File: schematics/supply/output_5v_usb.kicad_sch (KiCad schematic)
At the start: 88 parts, among them J2 USB_A, Q3 40N06, U10 IRS2153S, U11 CHY100, U12 LM2904, U13 LM2904, U15 LM2904, U16 AMS1117-3.3, U2 EL817, U3 TL431DBV, U4 TL431DBV, U6 INA3221, U8 MC34063AD

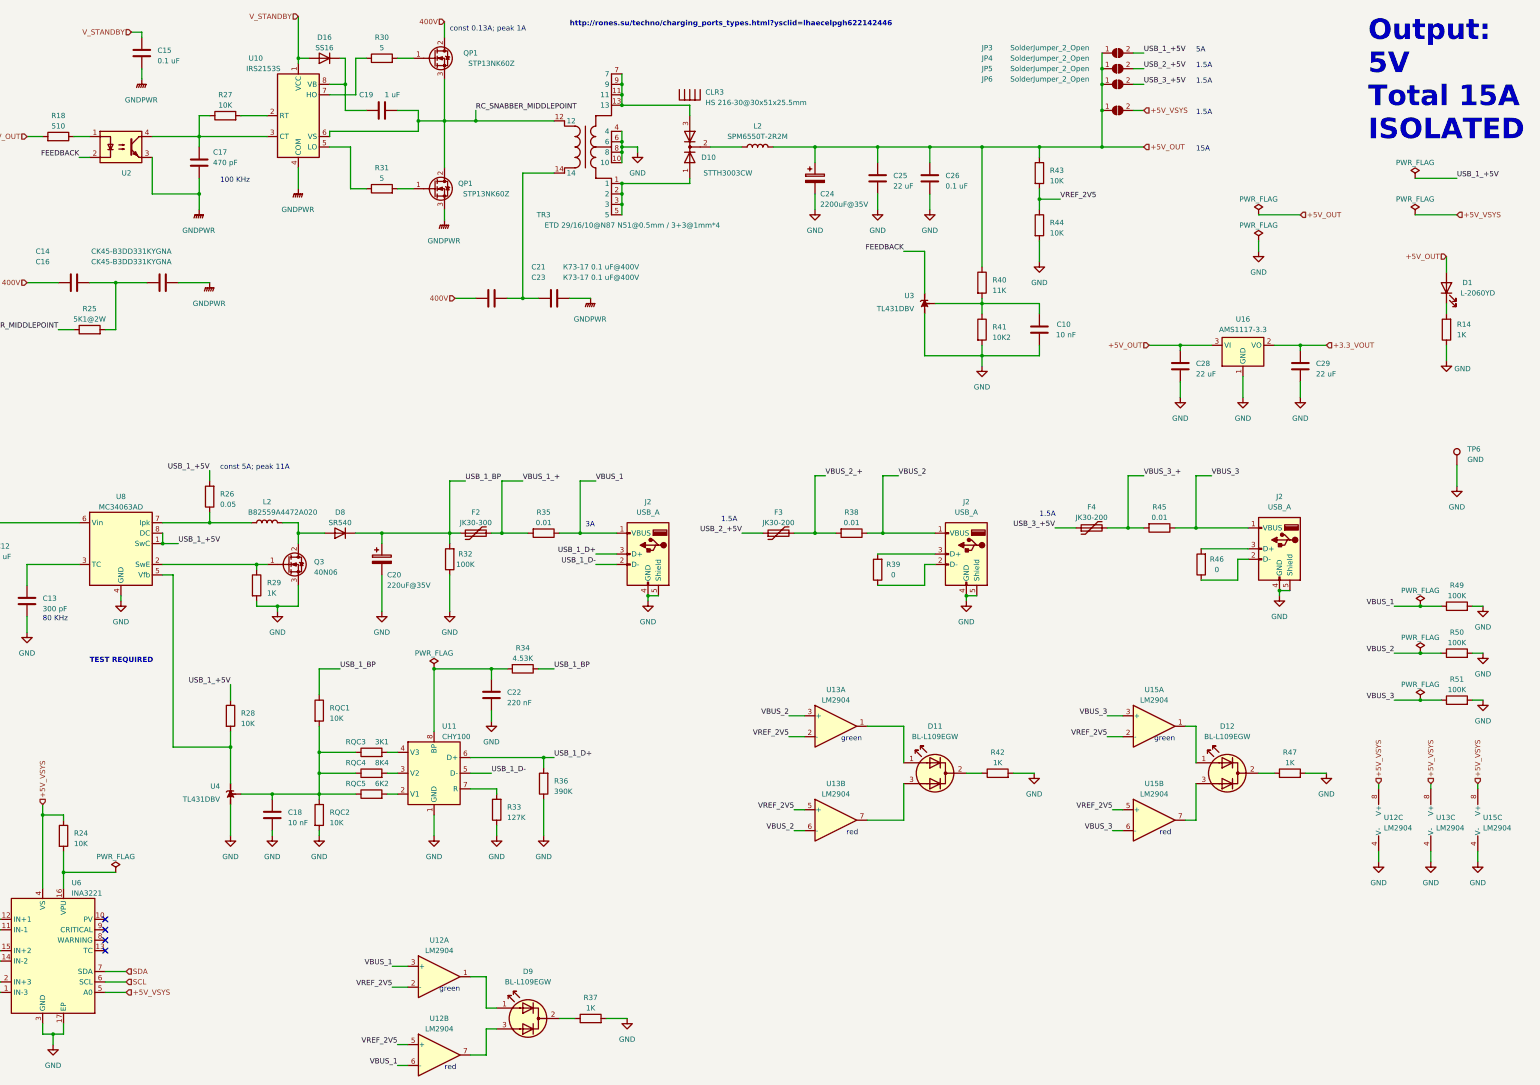
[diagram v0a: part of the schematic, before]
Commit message: prepare to replace ina228 to attiny16+ina169(?). ina228 is an intresting chip, but its too expensive and Im not sure I can buy it on ali
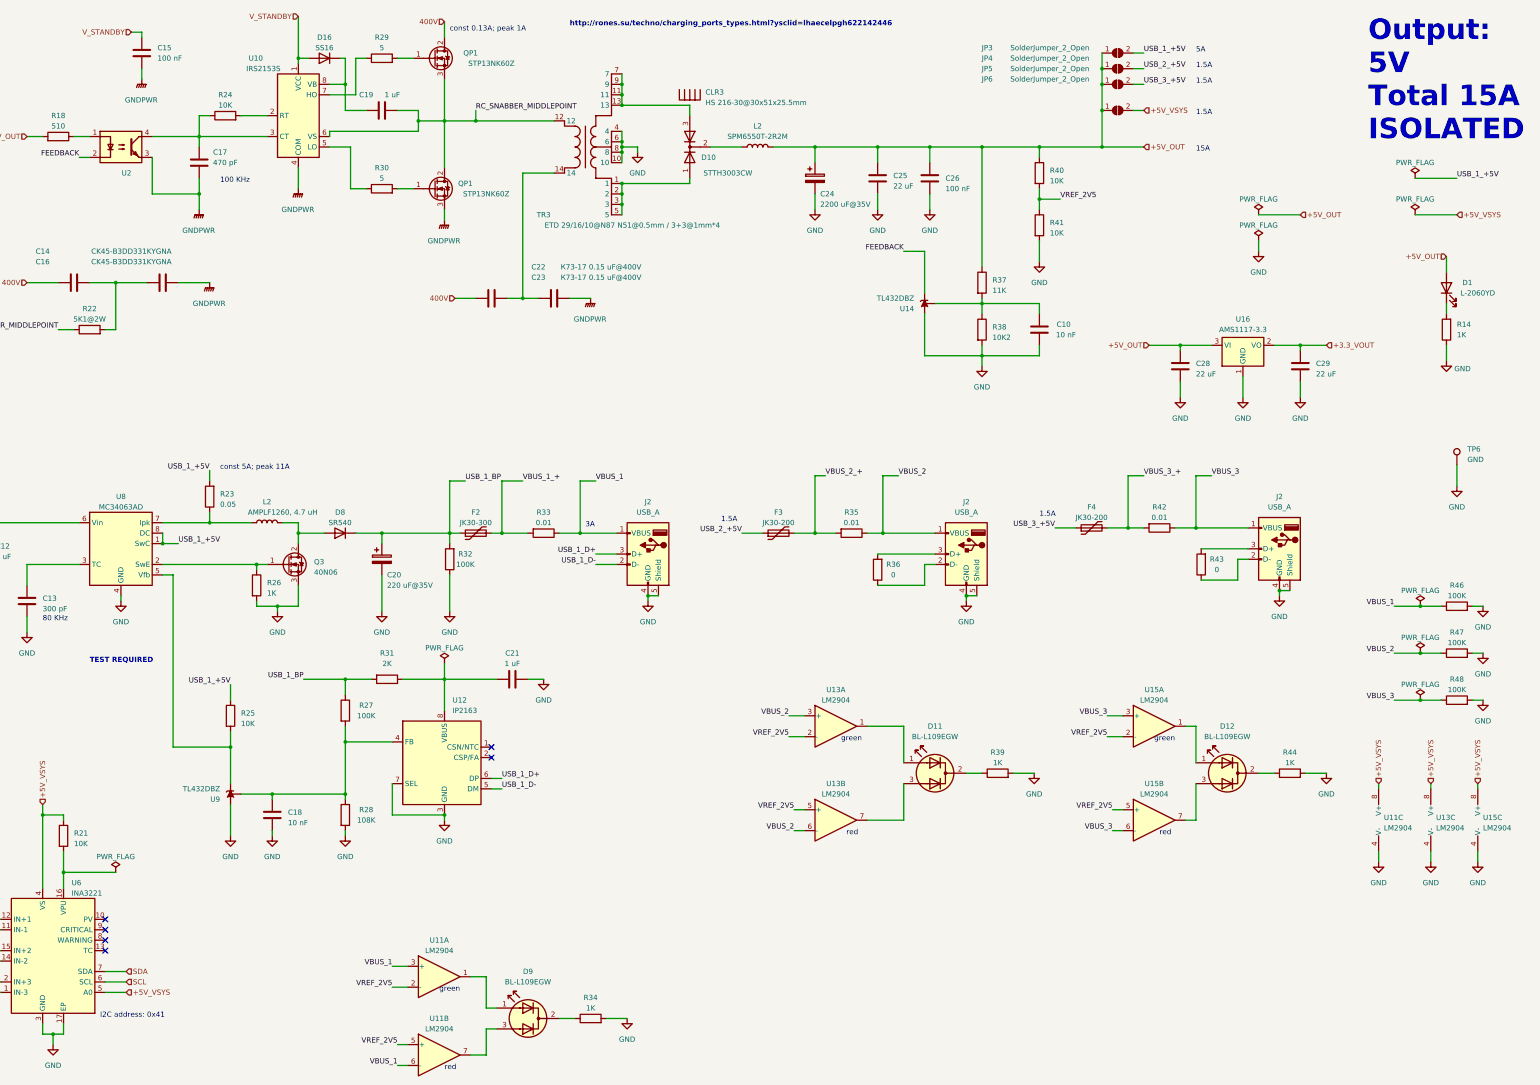
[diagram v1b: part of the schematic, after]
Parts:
- removed C22: 220 nF, Capacitor_SMD:C_0603_1608Metric, symbol Device:C
- removed R33: 127K, Resistor_SMD:R_0805_2012Metric, symbol Device:R
- removed R34: 4.53K, Resistor_SMD:R_0805_2012Metric, symbol Device:R
- removed R36: 390K, Resistor_SMD:R_0805_2012Metric, symbol Device:R
- removed RQC1, RQC2: 10K, Resistor_SMD:R_0805_2012Metric, symbol Device:R
- removed RQC3: 3K1, Resistor_SMD:R_0805_2012Metric, symbol Device:R
- removed RQC4: 8K4, Resistor_SMD:R_0805_2012Metric, symbol Device:R
- removed RQC5: 6K2, Resistor_SMD:R_0805_2012Metric, symbol Device:R
- removed U11: CHY100, Package_SO:SO-8_3.9x4.9mm_P1.27mm, symbol My_Library:CHY100
- removed U3, U4: TL431DBV, Package_TO_SOT_SMD:SOT-23-5, symbol Reference_Voltage:TL431DBV
- added C21: 1 uF, Capacitor_SMD:C_0603_1608Metric, symbol Device:C
- added R27: 100K, Resistor_SMD:R_0805_2012Metric, symbol Device:R
- added R28: 108K, Resistor_SMD:R_0805_2012Metric, symbol Device:R
- added R31: 2K, Resistor_SMD:R_0805_2012Metric, symbol Device:R
- added U12: IP2163, Package_SO:SOP-8_3.9x4.9mm_P1.27mm, symbol My_Library:IP2163
- added U14, U9: TL432DBZ, Package_TO_SOT_SMD:SOT-23-3, symbol Reference_Voltage:TL432DBZ
- C15, C26: value 0.1 uF -> 100 nF
- C20: value 220uF@35V -> 220 uF@35V
- C22: renamed from C21; value К73-17 0.1 uF@400V -> К73-17 0.15 uF@400V; footprint Capacitor_THT:C_Rect_L11.0mm_W6.3mm_P10.00mm_MKT -> Capacitor_THT:C_Rect_L16.5mm_W7.3mm_P15.00mm_MKT
- C23: value К73-17 0.1 uF@400V -> К73-17 0.15 uF@400V; footprint Capacitor_THT:C_Rect_L11.0mm_W6.3mm_P10.00mm_MKT -> Capacitor_THT:C_Rect_L16.5mm_W7.3mm_P15.00mm_MKT
- C24: value 2200uF@35V -> 2200 uF@35V
- D8: footprint Diode_THT:D_DO-27_P5.08mm_Vertical_KathodeUp -> Diode_THT:D_DO-201AD_P3.81mm_Vertical_KathodeUp
- L2: value B82559A4472A020 -> AMPLF1260, 4.7 uH; footprint Library:ERU 20 -> Inductor_SMD:L_TaiTech_TMPC1265_13.5x12.5mm
- U8: footprint Package_SO:SOIC-8_3.9x4.9mm_P1.27mm -> Package_SO:SOP-8_3.9x4.9mm_P1.27mm
- renumbered R24 to R21, R25 to R22, R26 to R23, R27 to R24, R28 to R25, R29 to R26, R30 to R29, R31 to R30, R35 to R33, R37 to R34, R38 to R35, R39 to R36, R40 to R37, R41 to R38, R42 to R39, R43 to R40, R44 to R41, R45 to R42, R46 to R43, R47 to R44, R49 to R46, R50 to R47, R51 to R48, U12 to U11
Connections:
- net FEEDBACK: now also U14.2 (K)
- net GND: now also C21.1, R28.2, U12.3 (GND), U12.7 (SEL), U14.3 (A), U9.3 (A)
- net USB_1_BP: now also R27.1, R31.2
- net USB_1_D+: now also U12.6 (DP)
- net USB_1_D-: now also U12.5 (DM)
- net at C18.2: now also R27.2, R28.1, U12.4 (FB), U9.1 (REF)
- net at R25.2, U8.5 (Vfb): now also U9.2 (K)
- net at C10.2, R37.2, R38.1: now also U14.1 (REF)
- new net: C21.2, R31.1, U12.8 (VBUS)
- no-connect marks 4 -> 6
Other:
- note added: "I2C address: 0x41"

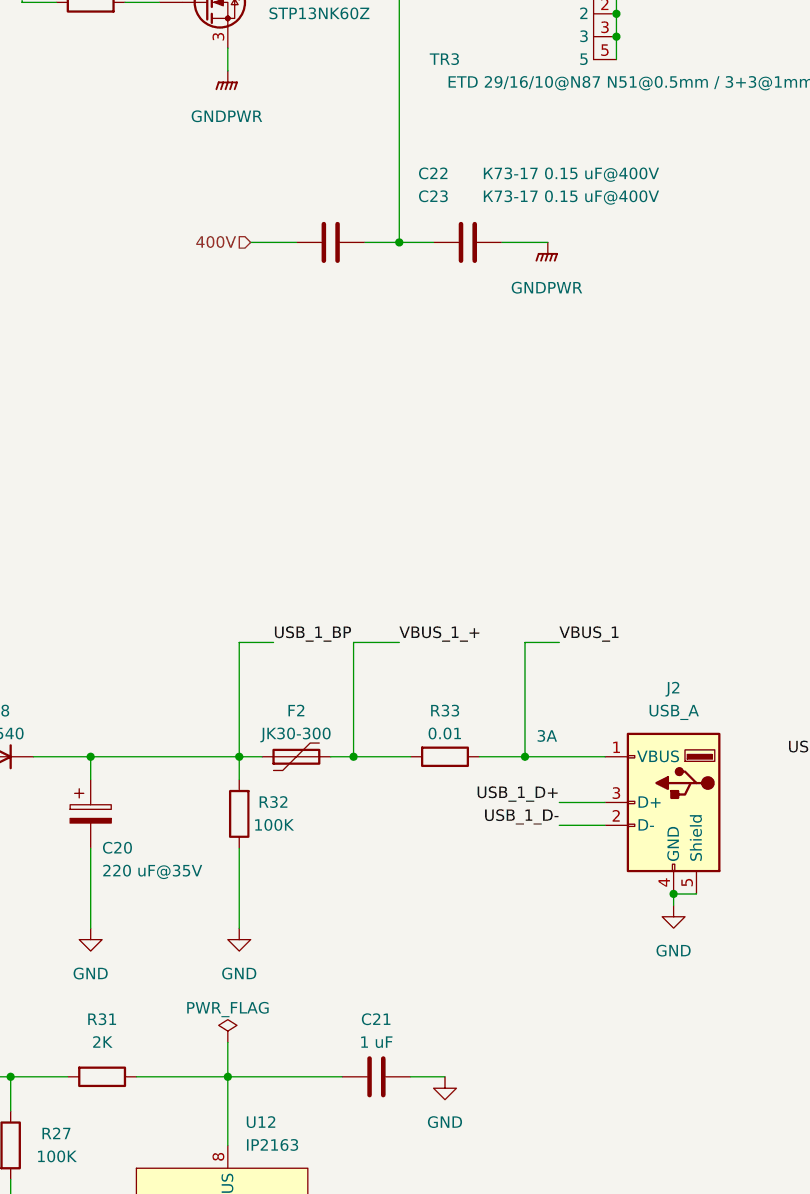
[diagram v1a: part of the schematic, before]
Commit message: Prepare to move USB ports to a few millimenters outside
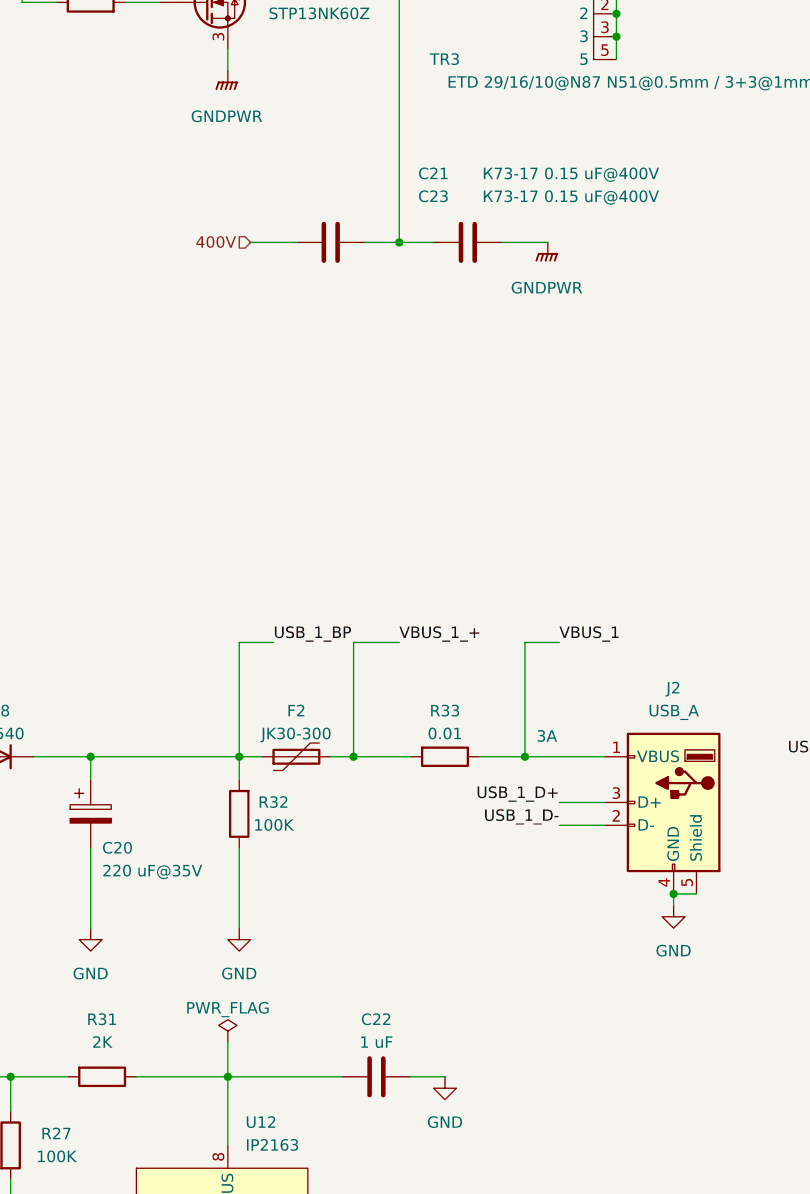
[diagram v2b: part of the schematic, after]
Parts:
- renumbered C22 to C21, C21 to C22
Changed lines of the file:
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@@
   (symbol (lib_id "Device:C") (at 156.21 85.09 270) (unit 1)
     (in_bom yes) (on_board yes) (dnp no)
-    (property "Reference" "C22" (at 167.64 77.47 90)
+    (property "Reference" "C21" (at 167.64 77.47 90)
       (effects (font (size 1.27 1.27)))
     )
@@
       (project "supply"
         (path "/1e139717-fcd1-4008-a6ea-4c993845e928/bcabd54f-a555-4409-9a4f-89c20a3d7682"
-          (reference "C22") (unit 1)
+          (reference "C21") (unit 1)
         )
       )
@@
   (symbol (lib_id "power:PWR_FLAG") (at 381 55.88 0) (unit 1)
     (in_bom yes) (on_board yes) (dnp no) (fields_autoplaced)
-    (property "Reference" "#FLG011" (at 381 53.975 0)
+    (property "Reference" "#FLG012" (at 381 53.975 0)
       (effects (font (size 1.27 1.27)) hide)
     )
@@
       (project "supply"
         (path "/1e139717-fcd1-4008-a6ea-4c993845e928/bcabd54f-a555-4409-9a4f-89c20a3d7682"
-          (reference "#FLG011") (unit 1)
+          (reference "#FLG012") (unit 1)
         )
       )
@@
   (symbol (lib_id "power:PWR_FLAG") (at 342.9 71.12 0) (unit 1)
     (in_bom yes) (on_board yes) (dnp no) (fields_autoplaced)
-    (property "Reference" "#FLG010" (at 342.9 69.215 0)
+    (property "Reference" "#FLG011" (at 342.9 69.215 0)
       (effects (font (size 1.27 1.27)) hide)
     )
@@
       (project "supply"
         (path "/1e139717-fcd1-4008-a6ea-4c993845e928/bcabd54f-a555-4409-9a4f-89c20a3d7682"
-          (reference "#FLG010") (unit 1)
+          (reference "#FLG011") (unit 1)
         )
       )
@@
   (symbol (lib_id "power:PWR_FLAG") (at 382.27 160.02 0) (unit 1)
     (in_bom yes) (on_board yes) (dnp no) (fields_autoplaced)
-    (property "Reference" "#FLG013" (at 382.27 158.115 0)
+    (property "Reference" "#FLG014" (at 382.27 158.115 0)
       (effects (font (size 1.27 1.27)) hide)
     )
@@
       (project "supply"
         (path "/1e139717-fcd1-4008-a6ea-4c993845e928/bcabd54f-a555-4409-9a4f-89c20a3d7682"
-          (reference "#FLG013") (unit 1)
+          (reference "#FLG014") (unit 1)
         )
       )
@@
   (symbol (lib_id "power:PWR_FLAG") (at 342.9 64.77 0) (unit 1)
     (in_bom yes) (on_board yes) (dnp no) (fields_autoplaced)
-    (property "Reference" "#FLG09" (at 342.9 62.865 0)
+    (property "Reference" "#FLG010" (at 342.9 62.865 0)
       (effects (font (size 1.27 1.27)) hide)
     )
@@
       (project "supply"
         (path "/1e139717-fcd1-4008-a6ea-4c993845e928/bcabd54f-a555-4409-9a4f-89c20a3d7682"
-          (reference "#FLG09") (unit 1)
+          (reference "#FLG010") (unit 1)
         )
       )
@@
   (symbol (lib_id "power:PWR_FLAG") (at 382.27 182.88 0) (unit 1)
     (in_bom yes) (on_board yes) (dnp no) (fields_autoplaced)
-    (property "Reference" "#FLG015" (at 382.27 180.975 0)
+    (property "Reference" "#FLG016" (at 382.27 180.975 0)
       (effects (font (size 1.27 1.27)) hide)
     )
@@
       (project "supply"
         (path "/1e139717-fcd1-4008-a6ea-4c993845e928/bcabd54f-a555-4409-9a4f-89c20a3d7682"
-          (reference "#FLG015") (unit 1)
+          (reference "#FLG016") (unit 1)
         )
       )
@@
   (symbol (lib_id "power:PWR_FLAG") (at 382.27 171.45 0) (unit 1)
     (in_bom yes) (on_board yes) (dnp no) (fields_autoplaced)
-    (property "Reference" "#FLG014" (at 382.27 169.545 0)
+    (property "Reference" "#FLG015" (at 382.27 169.545 0)
       (effects (font (size 1.27 1.27)) hide)
     )
@@
       (project "supply"
         (path "/1e139717-fcd1-4008-a6ea-4c993845e928/bcabd54f-a555-4409-9a4f-89c20a3d7682"
-          (reference "#FLG014") (unit 1)
+          (reference "#FLG015") (unit 1)
         )
       )
@@
   (symbol (lib_id "power:PWR_FLAG") (at 381 64.77 0) (unit 1)
     (in_bom yes) (on_board yes) (dnp no) (fields_autoplaced)
-    (property "Reference" "#FLG012" (at 381 62.865 0)
+    (property "Reference" "#FLG013" (at 381 62.865 0)
       (effects (font (size 1.27 1.27)) hide)
     )
@@
       (project "supply"
         (path "/1e139717-fcd1-4008-a6ea-4c993845e928/bcabd54f-a555-4409-9a4f-89c20a3d7682"
-          (reference "#FLG012") (unit 1)
+          (reference "#FLG013") (unit 1)
         )
       )
@@
   (symbol (lib_id "power:PWR_FLAG") (at 144.78 173.99 0) (unit 1)
     (in_bom yes) (on_board yes) (dnp no) (fields_autoplaced)
-    (property "Reference" "#FLG018" (at 144.78 172.085 0)
+    (property "Reference" "#FLG09" (at 144.78 172.085 0)
       (effects (font (size 1.27 1.27)) hide)
     )
@@
       (project "supply"
         (path "/1e139717-fcd1-4008-a6ea-4c993845e928/bcabd54f-a555-4409-9a4f-89c20a3d7682"
-          (reference "#FLG018") (unit 1)
+          (reference "#FLG09") (unit 1)
         )
       )
@@
   (symbol (lib_id "Device:C") (at 161.29 177.8 270) (unit 1)
     (in_bom yes) (on_board yes) (dnp no)
-    (property "Reference" "C21" (at 161.29 171.45 90)
+    (property "Reference" "C22" (at 161.29 171.45 90)
       (effects (font (size 1.27 1.27)))
     )
@@
       (project "supply"
         (path "/1e139717-fcd1-4008-a6ea-4c993845e928/bcabd54f-a555-4409-9a4f-89c20a3d7682"
-          (reference "C21") (unit 1)
-        )
-      )
+          (reference "C22") (unit 1)
+        )
+      )

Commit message: Updated boards
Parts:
- removed R23: 0.05, Resistor_SMD:R_0805_2012Metric, symbol Device:R
- D8: footprint Diode_THT:D_DO-201AD_P3.81mm_Vertical_KathodeUp -> Diode_THT:D_DO-201AD_P3.81mm_Vertical_AnodeUp
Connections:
- net USB_1_+5V: now also L2.1, U8.7 (Ipk)
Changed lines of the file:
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@@
     (stroke (width 0) (type default))
   )
-  (wire (pts (xy 87.63 137.16) (xy 87.63 139.7))
-    (stroke (width 0) (type default))
-  )
   (wire (pts (xy 154.94 257.81) (xy 157.48 257.81))
     (stroke (width 0) (type default))
@@
     (stroke (width 0) (type default))
   )
-  (wire (pts (xy 87.63 127) (xy 87.63 129.54))
-    (stroke (width 0) (type default))
-  )
   (wire (pts (xy 346.71 96.52) (xy 353.06 96.52))
     (stroke (width 0) (type default))
@@
     (stroke (width 0) (type default))
   )
+  (wire (pts (xy 87.63 127) (xy 87.63 139.7))
+    (stroke (width 0) (type default))
+  )
   (wire (pts (xy 121.92 58.42) (xy 125.73 58.42))
     (stroke (width 0) (type default))
@@
   (symbol (lib_id "Jumper:SolderJumper_2_Open") (at 308.61 33.02 0) (unit 1)
     (in_bom yes) (on_board yes) (dnp no)
-    (property "Reference" "JP5" (at 276.86 29.21 0)
+    (property "Reference" "JP5" (at 276.86 33.02 0)
       (effects (font (size 1.27 1.27)))
     )
-    (property "Value" "SolderJumper_2_Open" (at 292.1 29.21 0)
+    (property "Value" "SolderJumper_2_Open" (at 292.1 33.02 0)
       (effects (font (size 1.27 1.27)))
     )
@@
       (effects (font (size 1.27 1.27)))
     )
-    (property "Footprint" "Diode_THT:D_DO-201AD_P3.81mm_Vertical_KathodeUp" (at 119.38 142.24 0)
+    (property "Footprint" "Diode_THT:D_DO-201AD_P3.81mm_Vertical_AnodeUp" (at 119.38 142.24 0)
       (effects (font (size 1.27 1.27)) hide)
     )
@@
   (symbol (lib_id "Jumper:SolderJumper_2_Open") (at 308.61 29.21 0) (unit 1)
     (in_bom yes) (on_board yes) (dnp no)
-    (property "Reference" "JP4" (at 276.86 26.67 0)
+    (property "Reference" "JP4" (at 276.86 29.21 0)
       (effects (font (size 1.27 1.27)))
     )
-    (property "Value" "SolderJumper_2_Open" (at 292.1 26.67 0)
+    (property "Value" "SolderJumper_2_Open" (at 292.1 29.21 0)
       (effects (font (size 1.27 1.27)))
     )
@@
     )
   )
-  (symbol (lib_id "Device:R") (at 87.63 133.35 180) (unit 1)
-    (in_bom yes) (on_board yes) (dnp no) (fields_autoplaced)
-    (property "Reference" "R23" (at 90.17 132.715 0)
-      (effects (font (size 1.27 1.27)) (justify right))
-    )
-    (property "Value" "0.05" (at 90.17 135.255 0)
-      (effects (font (size 1.27 1.27)) (justify right))
-    )
-    (property "Footprint" "Resistor_SMD:R_0805_2012Metric" (at 89.408 133.35 90)
-      (effects (font (size 1.27 1.27)) hide)
-    )
-    (property "Datasheet" "~" (at 87.63 133.35 0)
-      (effects (font (size 1.27 1.27)) hide)
-    )
-    (pin "1")
-    (pin "2")
-    (instances
-      (project "supply"
-        (path "/1e139717-fcd1-4008-a6ea-4c993845e928/bcabd54f-a555-4409-9a4f-89c20a3d7682"
-          (reference "R23") (unit 1)
-        )
-      )
-    )
-  )
   (symbol (lib_id "power:PWR_FLAG") (at 342.9 71.12 0) (unit 1)
     (in_bom yes) (on_board yes) (dnp no) (fields_autoplaced)
@@
   (symbol (lib_id "Jumper:SolderJumper_2_Open") (at 308.61 25.4 0) (unit 1)
     (in_bom yes) (on_board yes) (dnp no)
-    (property "Reference" "JP3" (at 276.86 24.13 0)
+    (property "Reference" "JP3" (at 276.86 25.4 0)
       (effects (font (size 1.27 1.27)))
     )
-    (property "Value" "SolderJumper_2_Open" (at 292.1 24.13 0)
+    (property "Value" "SolderJumper_2_Open" (at 292.1 25.4 0)
       (effects (font (size 1.27 1.27)))
     )
@@
   (symbol (lib_id "Jumper:SolderJumper_2_Open") (at 308.61 39.37 0) (unit 1)
     (in_bom yes) (on_board yes) (dnp no)
-    (property "Reference" "JP6" (at 276.86 31.75 0)
+    (property "Reference" "JP6" (at 276.86 39.37 0)
       (effects (font (size 1.27 1.27)))
     )
-    (property "Value" "SolderJumper_2_Open" (at 292.1 31.75 0)
+    (property "Value" "SolderJumper_2_Open" (at 292.1 39.37 0)
       (effects (font (size 1.27 1.27)))
     )
